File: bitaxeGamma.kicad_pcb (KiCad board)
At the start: 4 copper layers, 56.5 x 99.8 mm, 146 parts, among them J1 54-00164, J2 TC2030-IDC, J3 Conn_01x04, J4 Conn_01x06, J5 USB_C_Receptacle_USB2.0, J6 Conn_01x04, SW1 GT-TC029B-H025-L1N, SW2 GT-TC029B-H025-L1N, T1 net-tie, U10 EMC2101, U2 TPS546D24ARVFR, U3 RT9080-33GJ5, U4 ESP32-S3-WROOM-1, U5 MCP1824T-1202E/OT, U6 MCP1824T-0802E, U7 25MHz, U8 BM1370_mode1, U9 SN74AVC4T774

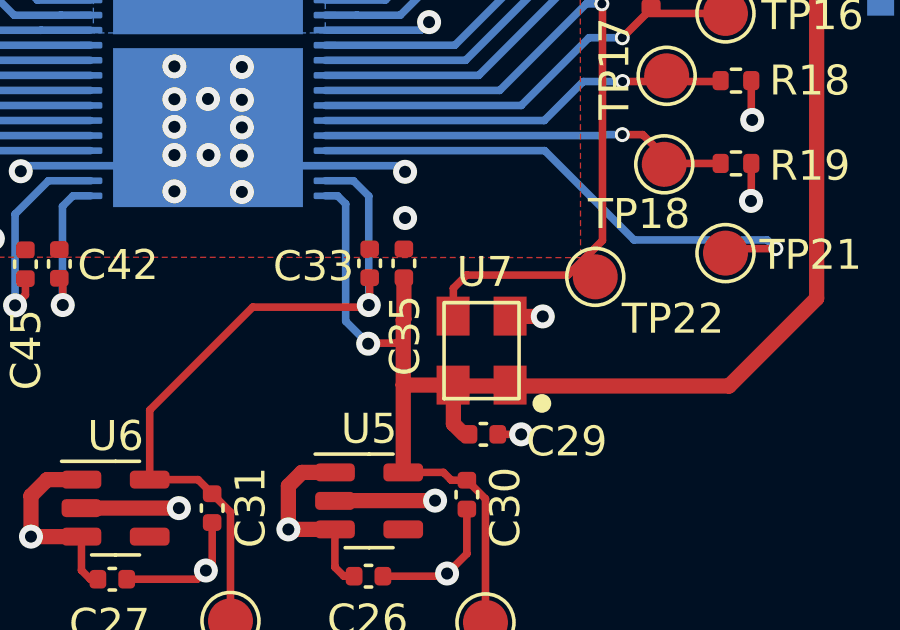
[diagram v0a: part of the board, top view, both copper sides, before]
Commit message: fix oscillator name
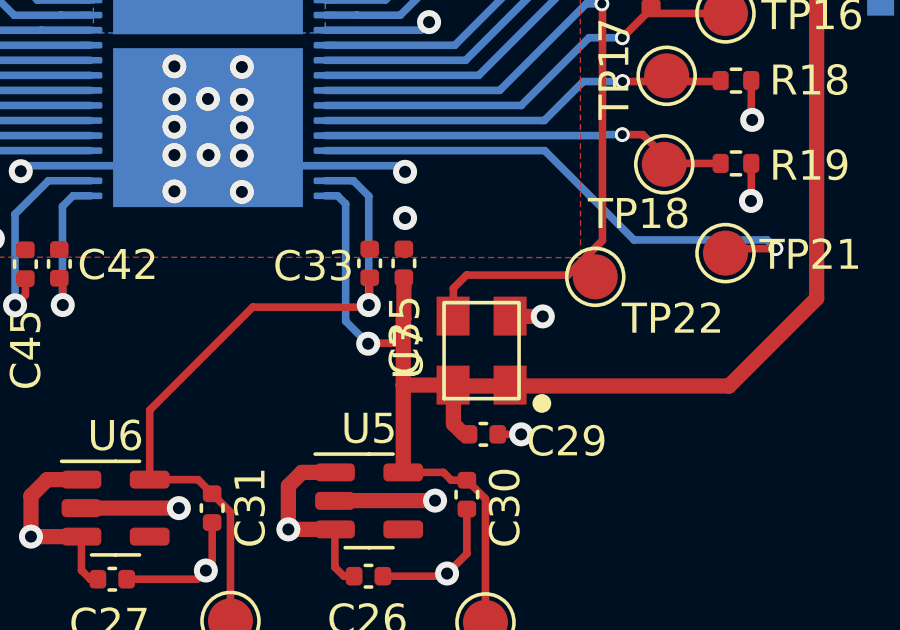
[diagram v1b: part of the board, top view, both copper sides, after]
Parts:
- U7: footprint bitaxe:O 25,0-JO32-B-1V3-1-T1-LF -> bitaxe:SMD3225-4P
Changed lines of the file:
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@@
 			)
 		)
-		(property "DK" "1276-1782-2-ND"
+		(property "DK" "1276-1782-1-ND"
 			(at 0 0 0)
 			(unlocked yes)
@@
 			)
 		)
-		(property "DK" "1276-1782-2-ND"
+		(property "DK" "1276-1782-1-ND"
 			(at 0 0 0)
 			(unlocked yes)
@@
 		)
 	)
-	(footprint "bitaxe:O 25,0-JO32-B-1V3-1-T1-LF"
+	(footprint "bitaxe:SMD3225-4P"
 		(layer "F.Cu")
 		(at 114.73 125.22 90)
 		(property "Reference" "U7"
-			(at 2.62 0.11 0)
+			(at -0.03 -2.43 90)
 			(unlocked yes)
 			(layer "F.SilkS")
@@
 			)
 		)
-		(property "Footprint" "bitaxe:O 25,0-JO32-B-1V3-1-T1-LF"
+		(property "Footprint" "bitaxe:SMD3225-4P"
 			(at 0 0 90)
 			(unlocked yes)
@@
 			)
 		)
-		(property "DK" "1276-1782-2-ND"
+		(property "DK" "1276-1782-1-ND"
 			(at 0 0 180)
 			(layer "F.Fab")
@@
 			)
 		)
-		(property "DK" "1276-1782-2-ND"
+		(property "DK" "1276-1782-1-ND"
 			(at 0 0 0)
 			(unlocked yes)
@@
 			)
 		)
-		(property "DK" "1276-1782-2-ND"
+		(property "DK" "1276-1782-1-ND"
 			(at 0 0 0)
 			(unlocked yes)

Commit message: bump version to 600
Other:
- board text added: "600"
- board text removed: "600x"
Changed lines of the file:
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@@
 		(at 114.73 125.22 90)
 		(property "Reference" "U7"
-			(at -0.03 -2.43 90)
+			(at 2.57 0.1 0)
 			(unlocked yes)
 			(layer "F.SilkS")
@@
 		)
 	)
-	(gr_text "600x"
+	(gr_text "600"
 		(at 105.83 84.94 0)
 		(layer "B.SilkS")

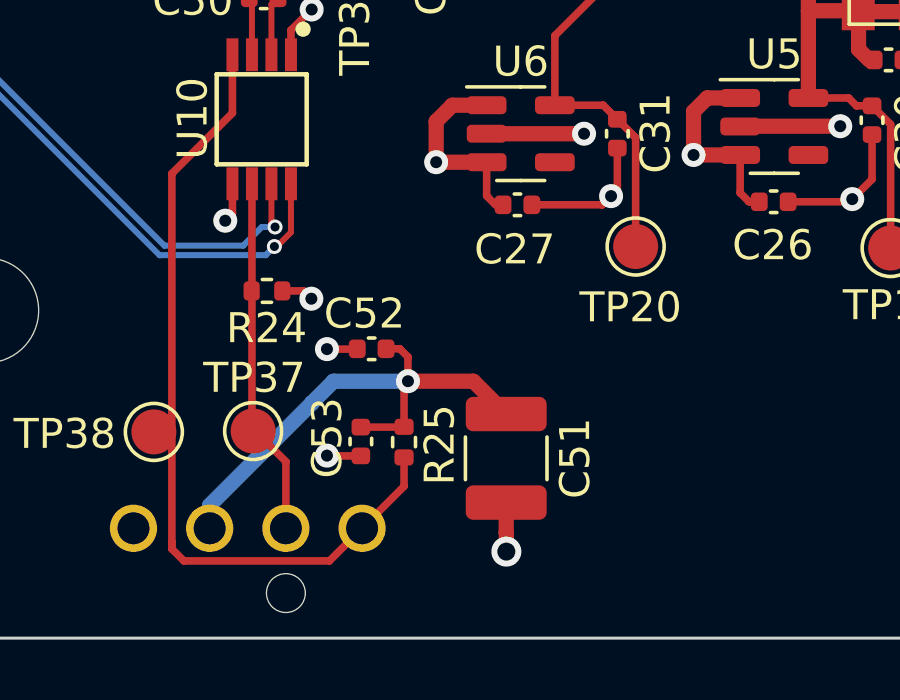
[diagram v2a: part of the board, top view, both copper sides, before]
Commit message: JST fan connector
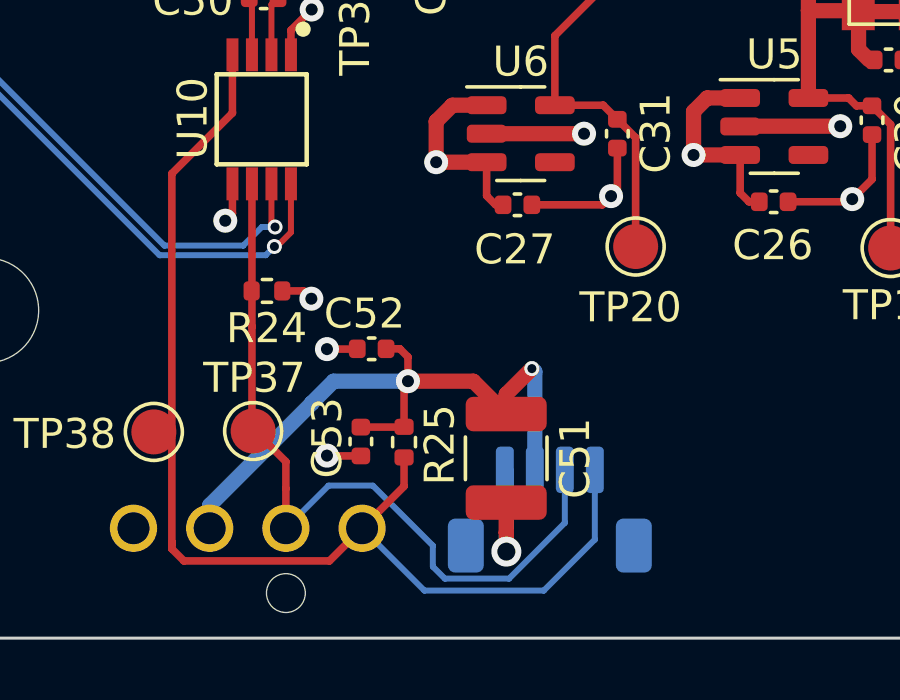
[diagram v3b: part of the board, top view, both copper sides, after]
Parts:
- added J7: Conn_01x04, Connector_JST:JST_SH_BM04B-SRSS-TB_1x04-1MP_P1.00mm_Vertical, B.Cu at (103.5, 143.0)
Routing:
- net /Fan/FAN_TACH: track 12.0 -> 26.1 mm
- net /Fan/FAN_PWM: track 27.4 -> 39.0 mm
- net /5V: track 191.5 -> 196.8 mm, vias 15 -> 16
- net GND: track 95.9 -> 98.7 mm
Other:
- board text added: "601"
- board text removed: "600"

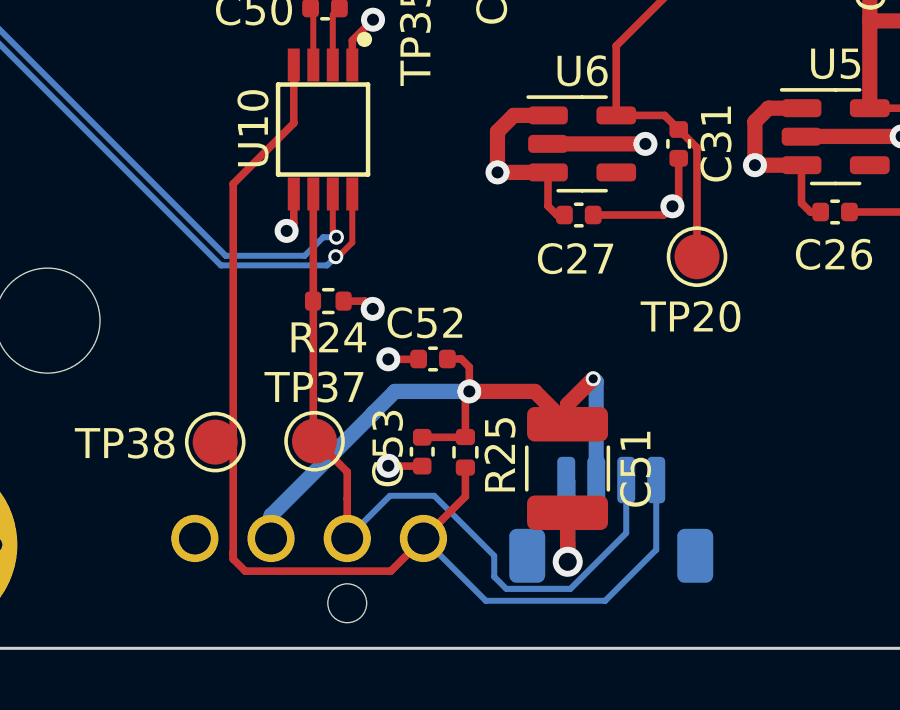
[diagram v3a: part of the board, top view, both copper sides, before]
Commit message: better fan routing
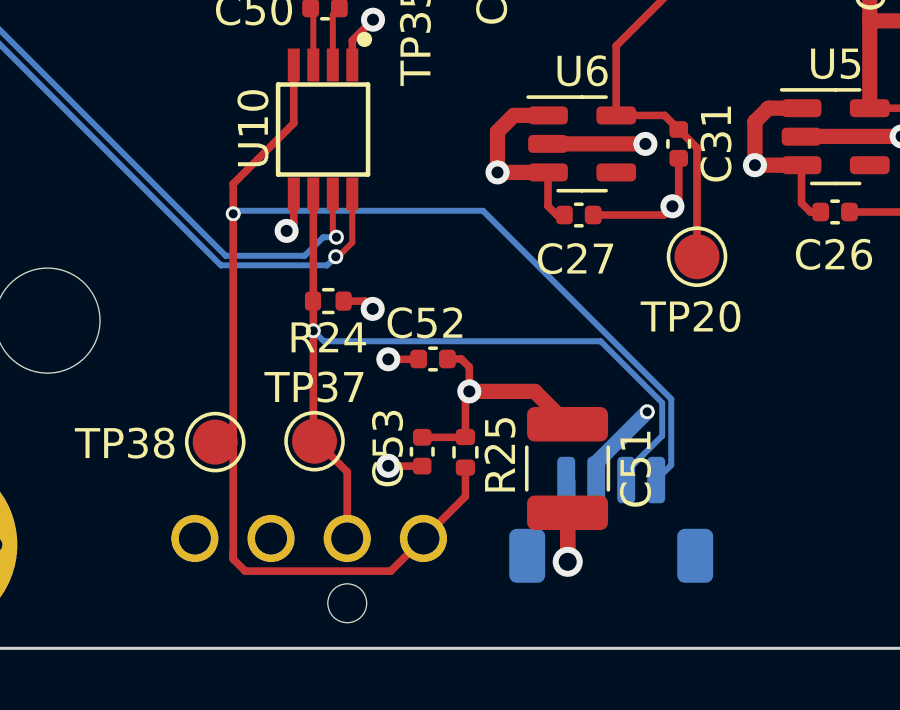
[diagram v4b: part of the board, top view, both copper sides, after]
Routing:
- net /Fan/FAN_PWM: track 39.0 -> 47.5 mm, vias 0 -> 1
- net /5V: track 196.8 -> 199.0 mm
- net /Fan/FAN_TACH: track 26.1 -> 27.6 mm, vias 0 -> 1
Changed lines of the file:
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@@
 	)
 	(segment
-		(start 102.045 139.155)
-		(end 102.045 139.815)
-		(width 0.508)
-		(layer "F.Cu")
-		(net 4)
-	)
-	(segment
 		(start 109.28 63.317)
 		(end 110.2828 64.3198)
@@
 	)
 	(segment
-		(start 102.9 138.3)
-		(end 102.045 139.155)
-		(width 0.508)
-		(layer "F.Cu")
-		(net 4)
-	)
-	(segment
 		(start 97.2 140.25)
 		(end 98.63 140.25)
@@
 	)
 	(via
-		(at 102.9 138.3)
-		(size 0.5)
-		(drill 0.3)
-		(layers "F.Cu" "B.Cu")
-		(net 4)
-	)
-	(via
 		(at 93.62 71.72)
 		(size 1)
@@
 		(net 4)
 	)
+	(via
+		(at 104.7 139.4)
+		(size 0.5)
+		(drill 0.3)
+		(layers "F.Cu" "B.Cu")
+		(net 4)
+	)
 	(segment
 		(start 92.3224 63.814606)
@@
 	)
 	(segment
+		(start 104.7 139.4)
+		(end 98.8 139.4)
+		(width 0.508)
+		(layer "In2.Cu")
+		(net 4)
+	)
+	(segment
 		(start 92.207 143.576)
 		(end 92.161 143.622)
@@
 	)
 	(segment
+		(start 98.8 139.4)
+		(end 93.06 139.4)
+		(width 0.508)
+		(layer "In2.Cu")
+		(net 4)
+	)
+	(segment
 		(start 92.161 143.622)
 		(end 92.161 138.501)
@@
 	)
 	(segment
+		(start 98.8 138.75)
+		(end 98.77 138.72)
+		(width 0.508)
+		(layer "In2.Cu")
+		(net 4)
+	)
+	(segment
 		(start 87.19 72.5748)
 		(end 92.3224 67.4424)
@@
 	)
 	(segment
+		(start 93.06 139.4)
+		(end 92.161 138.501)
+		(width 0.508)
+		(layer "In2.Cu")
+		(net 4)
+	)
+	(segment
 		(start 88.465 134.805)
 		(end 79.95 126.29)
@@
 	)
 	(segment
+		(start 98.8 139.4)
+		(end 98.8 138.75)
+		(width 0.508)
+		(layer "In2.Cu")
+		(net 4)
+	)
+	(segment
 		(start 96.586 51.054)
 		(end 99.171505 51.054)
@@
 	)
 	(segment
-		(start 92.161 142.859)
-		(end 92.161 143.622)
-		(width 0.508)
-		(layer "B.Cu")
-		(net 4)
-	)
-	(segment
-		(start 95.56 139.45)
-		(end 95.56 139.46)
+		(start 103 141.675)
+		(end 103 141.1)
 		(width 0.508)
 		(layer "B.Cu")
@@
 	)
 	(segment
-		(start 96.29 138.72)
-		(end 95.56 139.45)
-		(width 0.508)
-		(layer "B.Cu")
-		(net 4)
-	)
-	(segment
-		(start 98.77 138.72)
-		(end 96.29 138.72)
-		(width 0.508)
-		(layer "B.Cu")
-		(net 4)
-	)
-	(segment
-		(start 102.9 138.3)
-		(end 103 138.4)
-		(width 0.508)
-		(layer "B.Cu")
-		(net 4)
-	)
-	(segment
-		(start 103 138.4)
-		(end 103 141.675)
+		(start 103 141.1)
+		(end 104.7 139.4)
 		(width 0.508)
 		(layer "B.Cu")
@@
 	)
 	(segment
-		(start 95.56 139.46)
-		(end 92.161 142.859)
-		(width 0.508)
-		(layer "B.Cu")
-		(net 4)
-	)
-	(segment
 		(start 126 84.5)
 		(end 126.06 84.56)
@@
 	)
 	(segment
+		(start 90.9 144.09)
+		(end 90.9 132.8)
+		(width 0.254)
+		(layer "F.Cu")
+		(net 11)
+	)
+	(segment
 		(start 90.9 144.1716)
 		(end 90.9 144.09)
@@
 	(segment
 		(start 90.9 144.09)
-		(end 90.9 131.8)
-		(width 0.254)
-		(layer "F.Cu")
-		(net 11)
-	)
-	(segment
-		(start 90.9 144.09)
 		(end 90.9 144.31)
 		(width 0.254)
@@
 	)
 	(segment
+		(start 90.9 132.8)
+		(end 90.9 131.8)
+		(width 0.254)
+		(layer "F.Cu")
+		(net 11)
+	)
+	(segment
 		(start 90.9 144.31)
 		(end 91.3 144.71)
@@
 		(net 11)
 	)
+	(via
+		(at 90.9 132.8)
+		(size 0.5)
+		(drill 0.3)
+		(layers "F.Cu" "B.Cu")
+		(net 11)
+	)
+	(segment
+		(start 105.5016 138.975074)
+		(end 99.226526 132.7)
+		(width 0.2)
+		(layer "B.Cu")
+		(net 11)
+	)
 	(segment
-		(start 97.241 143.622)
-		(end 99.319 145.7)
+		(start 99.226526 132.7)
+		(end 91 132.7)
 		(width 0.2)
 		(layer "B.Cu")
@@
 	)
 	(segment
-		(start 99.319 145.7)
-		(end 103.3 145.7)
+		(start 105 141.675)
+		(end 105.5016 141.1734)
 		(width 0.2)
 		(layer "B.Cu")
@@
 	)
 	(segment
-		(start 105 144)
-		(end 105 141.675)
+		(start 91 132.7)
+		(end 90.9 132.8)
 		(width 0.2)
 		(layer "B.Cu")
@@
 	)
 	(segment
-		(start 103.3 145.7)
-		(end 105 144)
+		(start 105.5016 141.1734)
+		(end 105.5016 138.975074)
 		(width 0.2)
 		(layer "B.Cu")
@@
 	)
 	(segment
-		(start 94.701 141.401)
-		(end 94.701 142.3)
+		(start 93.57 136.7)
+		(end 93.57 132.14)
 		(width 0.254)
 		(layer "F.Cu")
@@
 	)
 	(segment
-		(start 93.57 136.9)
+		(start 93.57 136.7)
 		(end 93.57 140.27)
 		(width 0.254)
@@
 	)
 	(segment
-		(start 93.57 132.14)
-		(end 93.57 136.9)
-		(width 0.254)
-		(layer "F.Cu")
-		(net 101)
-	)
-	(segment
-		(start 94.701 142.3)
+		(start 94.701 141.401)
 		(end 94.701 143.622)
 		(width 0.254)
@@
 		(net 101)
 	)
-	(segment
-		(start 97.6 142.2)
-		(end 96.123 142.2)
-		(width 0.2)
-		(layer "B.Cu")
-		(net 101)
-	)
-	(segment
-		(start 99.6 144.2)
-		(end 97.6 142.2)
-		(width 0.2)
-		(layer "B.Cu")
+	(via
+		(at 93.57 136.7)
+		(size 0.5)
+		(drill 0.3)
+		(layers "F.Cu" "B.Cu")
 		(net 101)
 	)
 	(segment
-		(start 96.123 142.2)
-		(end 94.701 143.622)
+		(start 105.2 140.198606)
+		(end 104 141.398606)
 		(width 0.2)
 		(layer "B.Cu")
@@
 	)
 	(segment
-		(start 99.6 144.9)
-		(end 99.6 144.2)
+		(start 93.9184 137.0484)
+		(end 103.1484 137.0484)
 		(width 0.2)
 		(layer "B.Cu")
@@
 	)
 	(segment
-		(start 100.0016 145.3016)
-		(end 99.6 144.9)
+		(start 105.2 139.1)
+		(end 105.2 140.198606)
 		(width 0.2)
 		(layer "B.Cu")
@@
 	)
 	(segment
-		(start 104 143.442213)
-		(end 102.140613 145.3016)
+		(start 103.1484 137.0484)
+		(end 105.2 139.1)
 		(width 0.2)
 		(layer "B.Cu")
@@
 	)
 	(segment
-		(start 102.140613 145.3016)
-		(end 100.0016 145.3016)
+		(start 104 141.398606)
+		(end 104 141.675)
 		(width 0.2)
 		(layer "B.Cu")
@@
 	)
 	(segment
-		(start 104 141.675)
-		(end 104 143.442213)
+		(start 93.57 136.7)
+		(end 93.9184 137.0484)
 		(width 0.2)
 		(layer "B.Cu")

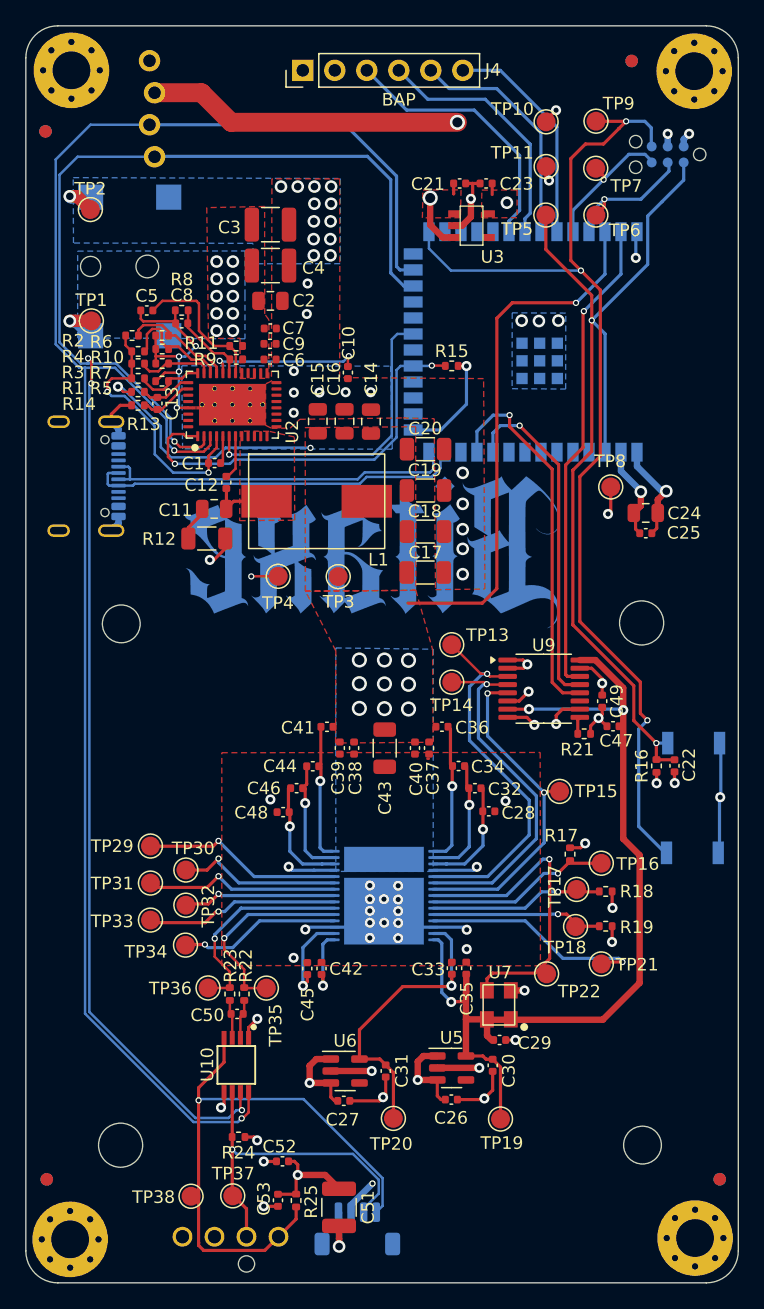
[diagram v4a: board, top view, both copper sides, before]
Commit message: fan routing and MP anchor
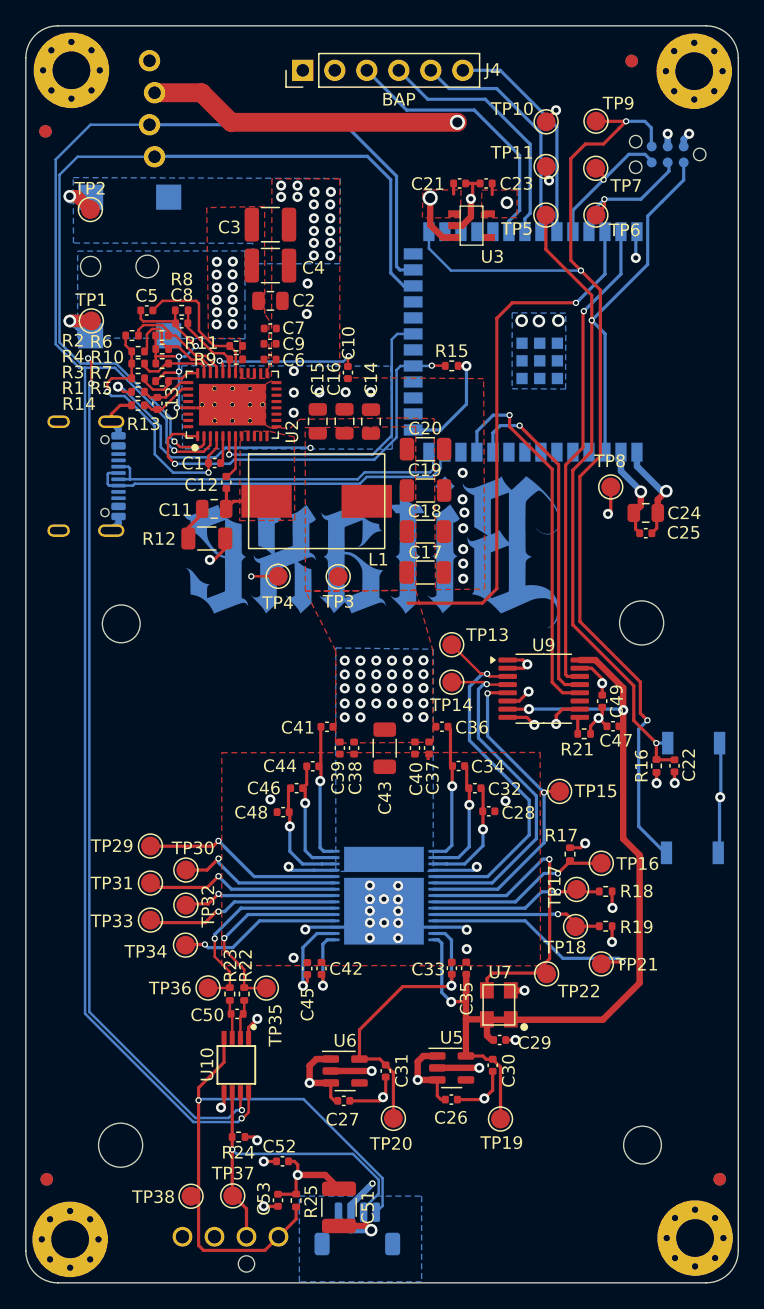
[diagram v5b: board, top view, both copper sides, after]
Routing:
- net GND: track 98.7 -> 100.5 mm, vias 76 -> 82
- net /VDD: vias 12 -> 31
- net /5V: vias 16 -> 18
- added copper zone on B.Cu, net unconnected-(J7-MountPin-PadMP)

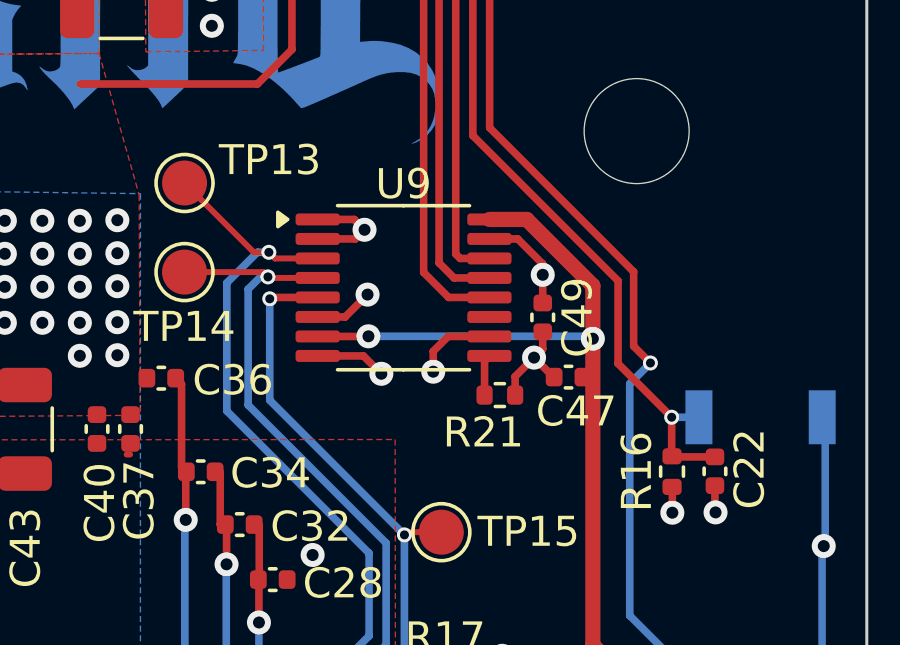
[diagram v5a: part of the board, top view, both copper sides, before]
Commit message: bump version to 602. remove R21 and fix for #6
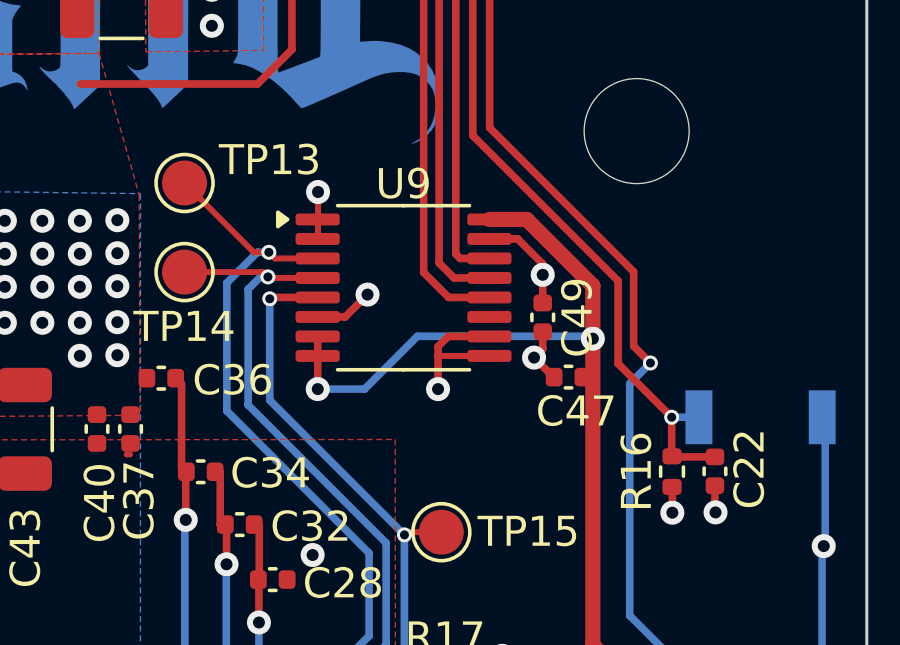
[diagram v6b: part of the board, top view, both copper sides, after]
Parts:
- removed R21: 20k, Resistor_SMD:R_0402_1005Metric
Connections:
- U9 pad 8: GND -> /BM1370/1V2
- U9 pad 9: Net-(U9-OE) -> GND
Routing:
- net GND: track 100.5 -> 97.0 mm, vias 82 -> 81
- net /BM1370/1V2: track 74.6 -> 77.1 mm
- net Net-(U9-OE): track 1.37 -> 0.00 mm
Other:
- board text added: "602"
- board text removed: "601"
